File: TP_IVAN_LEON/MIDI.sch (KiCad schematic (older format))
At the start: 6 parts, among them P6 DIN_5

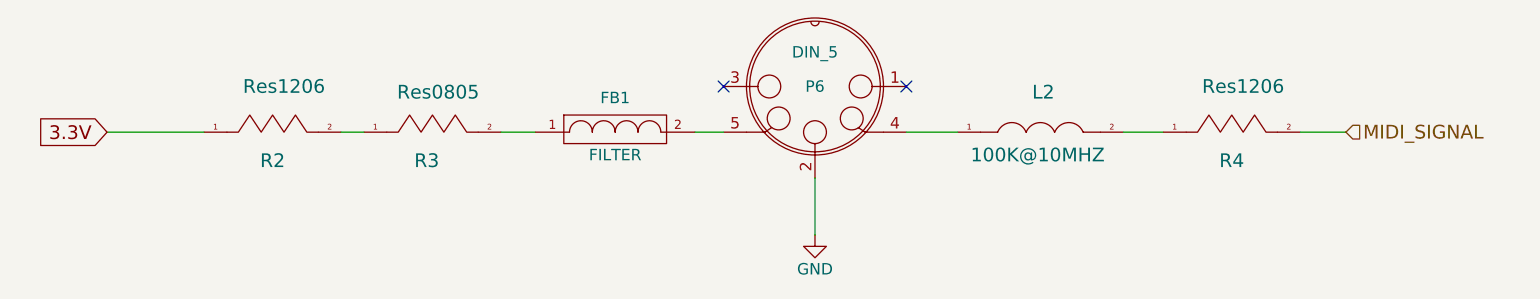
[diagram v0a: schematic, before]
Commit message: Agregado codigo digey key en 80% de componentes
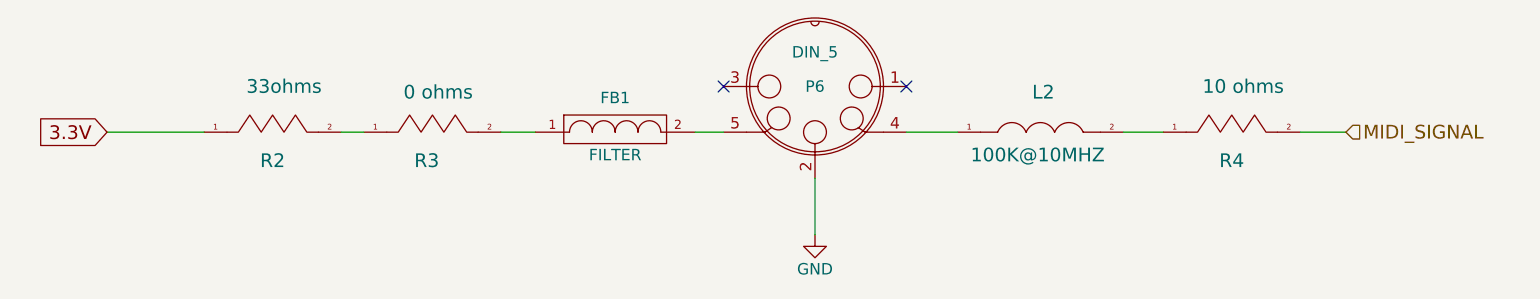
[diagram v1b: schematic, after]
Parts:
- FB1, L2: Digikey# (none) -> 732-10154-ND
- P6: Digikey# (none) -> CP-2350-ND
- R2: value Res1206 -> 33ohms; Digikey# (none) -> 311-33ERTR-ND
- R3: value Res0805 -> 0 ohms; Digikey# (none) -> 541-2970-6-ND
- R4: value Res1206 -> 10 ohms; Digikey# (none) -> YAG1337TR-ND
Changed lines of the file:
@@
 F 2 "TP:Choke_SMD_1206_Standard" H 6575 2975 60  0001 C CNN
 F 3 "" H 6575 2975 60  0000 C CNN
+F 4 "732-10154-ND" H 6575 2975 60  0001 C CNN "Digikey#"
 	1    6575 2975
 	1    0    0    -1
@@
 P 3900 2975
 F 0 "R3" H 3900 2850 60  0000 C CNN
-F 1 "Res0805" H 3950 3150 60  0000 C CNN
+F 1 "0 ohms" H 3950 3150 60  0000 C CNN
 F 2 "TP:Resistor_SMD+THTuniversal_0805to2512_RM10_HandSoldering" H 3900 2975 60  0001 C CNN
 F 3 "" H 3900 2975 60  0000 C CNN
+F 4 "541-2970-6-ND" H 3900 2975 60  0001 C CNN "Digikey#"
 	1    3900 2975
 	1    0    0    -1
@@
 P 3200 2975
 F 0 "R2" H 3225 2850 60  0000 C CNN
-F 1 "Res1206" H 3275 3175 60  0000 C CNN
+F 1 "33ohms" H 3275 3175 60  0000 C CNN
 F 2 "TP:Resistor_SMD+THTuniversal_1206_RM10_HandSoldering" H 3200 2975 60  0001 C CNN
 F 3 "" H 3200 2975 60  0000 C CNN
+F 4 "311-33ERTR-ND" H 3200 2975 60  0001 C CNN "Digikey#"
 	1    3200 2975
 	1    0    0    -1
@@
 P 7400 2975
 F 0 "R4" H 7425 2850 60  0000 C CNN
-F 1 "Res1206" H 7475 3175 60  0000 C CNN
+F 1 "10 ohms" H 7475 3175 60  0000 C CNN
 F 2 "TP:Resistor_SMD+THTuniversal_1206_RM10_HandSoldering" H 7400 2975 60  0001 C CNN
 F 3 "" H 7400 2975 60  0000 C CNN
+F 4 "YAG1337TR-ND" H 7400 2975 60  0001 C CNN "Digikey#"
 	1    7400 2975
 	1    0    0    -1
@@
 F 2 "TP:din-5" H 5600 2775 50  0001 C CNN
 F 3 "" H 5600 2775 50  0000 C CNN
+F 4 "CP-2350-ND" H 5600 2775 60  0001 C CNN "Digikey#"
 	1    5600 2775
 	-1   0    0    1
@@
 F 2 "TP:Choke_SMD_1206_Standard" H 4725 2975 50  0001 C CNN
 F 3 "" H 4725 2975 50  0000 C CNN
+F 4 "732-10154-ND" H 4725 2975 60  0001 C CNN "Digikey#"
 	1    4725 2975
 	1    0    0    -1
